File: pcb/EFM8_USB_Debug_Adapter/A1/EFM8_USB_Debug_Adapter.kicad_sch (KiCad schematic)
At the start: 27 parts, among them J100 EFM8 IDC Debug Header, J101 Conn_01x06, J110 2137160001, J120 31230102, J130 EFM8 USB 8-Bit Debug Header, J131 Conn_01x02_Male, Q110 SI3443CDV-T1-GE3, Q111 DMMT5401, Q120 SI3443CDV-T1-GE3, Q121 DMMT5401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

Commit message: Erstes Layout
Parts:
- removed J101: Conn_01x06, Connector_PinHeader_2.54mm:PinHeader_1x06_P2.54mm_Vertical, symbol Connector_Generic:Conn_01x06
- added J111: TTL-232R Header, Connector_PinHeader_2.54mm:PinHeader_1x06_P2.54mm_Vertical, symbol Connector_Special_Purpose_User:TTL-232R Header
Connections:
- net GND: now also J111.1 (GND)
- net UART_RX: now also J111.5 (RXD)
- net UART_TX: now also J111.4 (TXD)

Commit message: PCB bearbeitet, FreeCAD Projet angelegt
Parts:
- removed F110: 0805L110SLxx, Fuse:Fuse_0805_2012Metric_Pad1.15x1.40mm_HandSolder, symbol Fuse_User:0805L110SLxx
- removed J131: Conn_01x02_Male, Connector_PinHeader_2.54mm:PinHeader_1x02_P2.54mm_Vertical, symbol Connector:Conn_01x02_Male
- added D111, D121, D131: 150080SS75000, LED_SMD:LED_0805_2012Metric_Pad1.15x1.40mm_HandSolder, symbol LED_User:150080SS75000
- added F110: 0ZCJ0110FF2E, Fuse:Fuse_1206_3216Metric_Pad1.42x1.75mm_HandSolder, symbol Fuse_User:0ZCJ0110FF2E
- added JP130: SolderJumper_2_Bridged, Jumper:SolderJumper-2_P1.3mm_Bridged_RoundedPad1.0x1.5mm, symbol Jumper:SolderJumper_2_Bridged
- added R115, R123, R133: 2k,0603, Resistor_SMD:R_0603_1608Metric_Pad0.98x0.95mm_HandSolder, symbol Resistor_User:2k,0603
- D110, D120, D130: value LTST-C191TGKT -> 150080SS75000; footprint LED_SMD:LED_0603_1608Metric_Pad1.05x0.95mm_HandSolder -> LED_SMD:LED_0805_2012Metric_Pad1.15x1.40mm_HandSolder; symbol LED_User:LTST-C191TGKT -> LED_User:150080SS75000; Info Green -> Red; Manufacturer Lite-On -> Wurth Elektronik; SPN 160-1888-1-ND -> 732-4985-1-ND
- J100: value EFM8 IDC Debug Header -> EFM8_IDC_Debug_Header_Horizontal; footprint Connector_User:IDC-Header_2x03_P2.54mm_Vertical_61200621621 -> Connector_User:IDC-Header_2x03_P2.54mm_Horizontal_61200621721; symbol Connector_Special_Purpose_User:EFM8 IDC Debug Header -> Connector_Special_Purpose_User:EFM8_IDC_Debug_Header_Horizontal; MPN 61200621621 -> 61200621721; SPN 732-5394-ND -> 732-5404-ND
- J111: value TTL-232R Header -> TTL-232R_Header_Horizontal; footprint Connector_PinHeader_2.54mm:PinHeader_1x06_P2.54mm_Vertical -> Connector_PinHeader_2.54mm:PinHeader_1x06_P2.54mm_Horizontal; symbol Connector_Special_Purpose_User:TTL-232R Header -> Connector_Special_Purpose_User:TTL-232R_Header_Horizontal; MPN 61300611121 -> 61300611021; Pretty Value 1 01x06 Header -> 01x06 Header, Vertical; SPN 732-5319-ND -> 732-5339-ND
- J130: value EFM8 USB 8-Bit Debug Header -> EFM8_USB_8-Bit_Debug_Header_Horizontal; footprint Connector_User:IDC-Header_2x05_P2.54mm_Vertical_61201021621 -> Connector_User:IDC-Header_2x05_P2.54mm_Horizontal_61201021721; symbol Connector_Special_Purpose_User:EFM8 USB 8-Bit Debug Header -> Connector_Special_Purpose_User:EFM8_USB_8-Bit_Debug_Header_Horizontal; MPN 61201021621 -> 61201021721; SPN 732-2094-ND -> 732-2098-ND
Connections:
- net Ext_PSU_Power: now also D121.2 (A)
- net Ext_USB_Power: now also F110.1
- net GND: now also R115.2, R123.2, R133.2
- net Prog_USB_Power: now also JP130.1 (A)
- net Ext_USB_Power_Fused: now reaches D110.2 (A), Q110.1 (D), Q110.2 (D), Q110.5 (D), Q110.6 (D), Q111.6 (E1)
- net Ext_USB_Power_Fused: now also D111.2 (A), F110.2
- net at D130.2 (A), Q130.1 (D), Q130.2 (D)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: now also D131.2 (A), JP130.2 (B)
- new net: D131.1 (K), R133.1
- new net: D121.1 (K), R123.1
- new net: D111.1 (K), R115.1
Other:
- moved on the sheet: D110, D120, D130, J100, J110, J111, J120, J130, Q110, Q111, Q120, Q121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

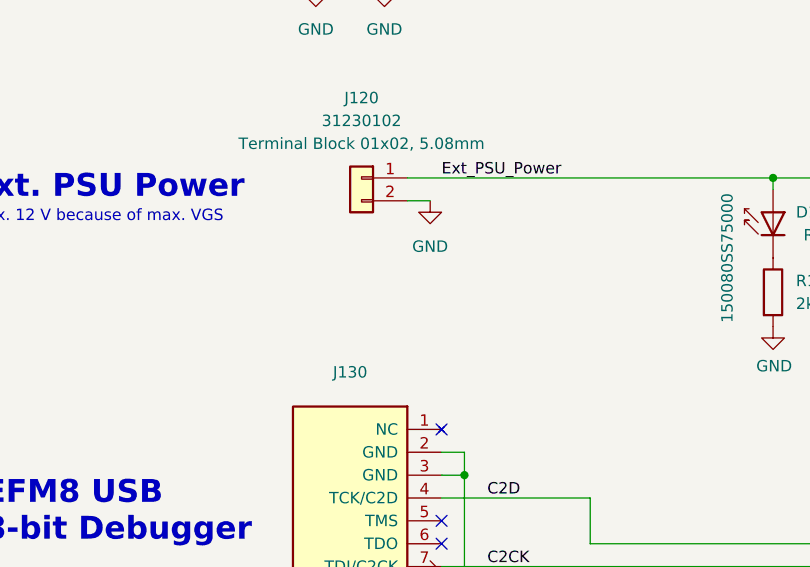
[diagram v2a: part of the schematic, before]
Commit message: Gehäuse bearbeitet
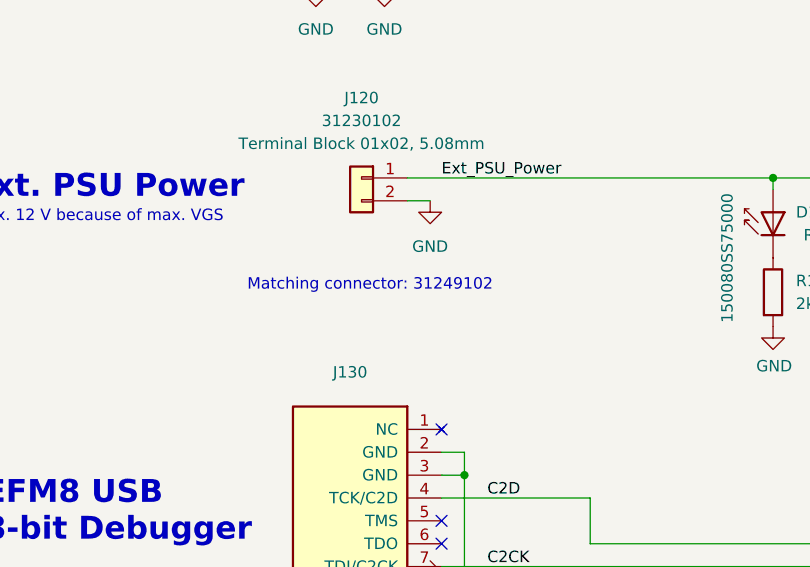
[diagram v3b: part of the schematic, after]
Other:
- note added: "Matching connector: 31249102"
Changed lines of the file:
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@@
+    (effects (font (size 1.27 1.27)) (justify left bottom))
+  )
+  (text "Matching connector: 31249102" (at 44.45 95.25 0)
     (effects (font (size 1.27 1.27)) (justify left bottom))
   )
@@
       (effects (font (size 1.27 1.27)) hide)
     )
-    (property "Datasheet" "https://www.metz-connect.com/html/overlay:service:download.en.html?filepath=db%3Aproducts%2Fdocid%3A8a8a80ea821fbff0018315b584d92138.de.1&fileurl=312301%2F873130.PDF" (id 3) (at 57.15 100.33 0)
-      (effects (font (size 1.27 1.27)) hide)
-    )
+    (property "Datasheet" "https://www.metz-connect.com/externalfiles/312301/873130.PDF" (id 3) (at 57.15 100.33 0)
+      (effects (font (size 1.27 1.27)) hide)
+    )

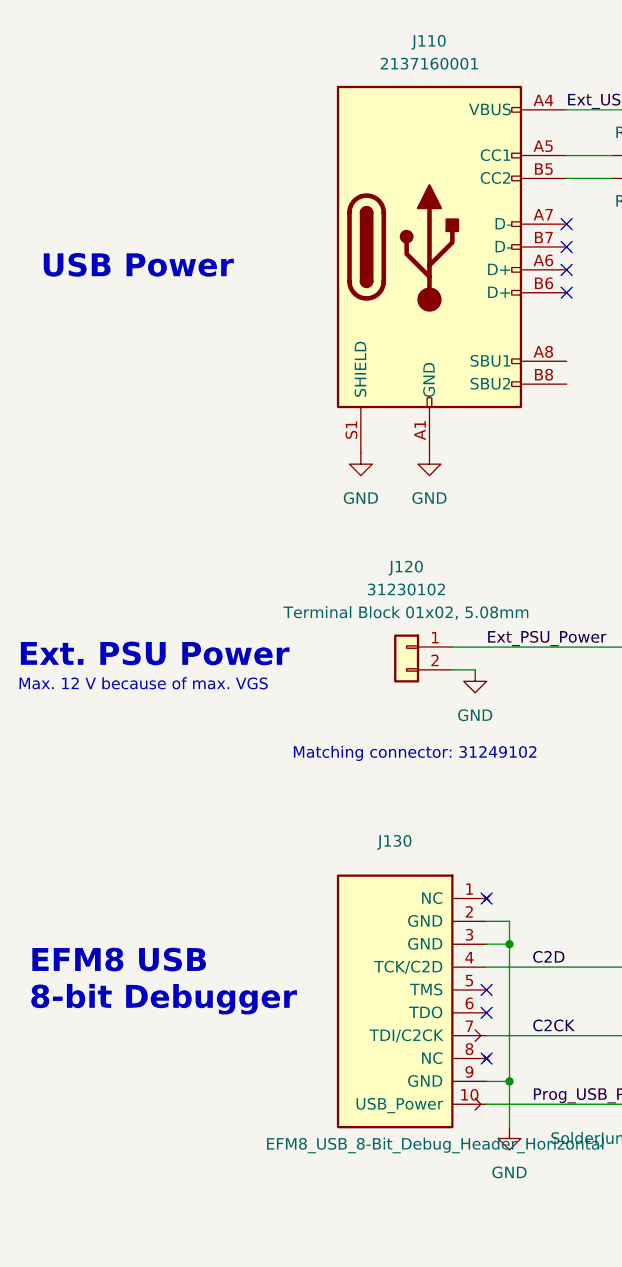
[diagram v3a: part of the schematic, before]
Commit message: Light Pipes in KiCad hinzugefügt
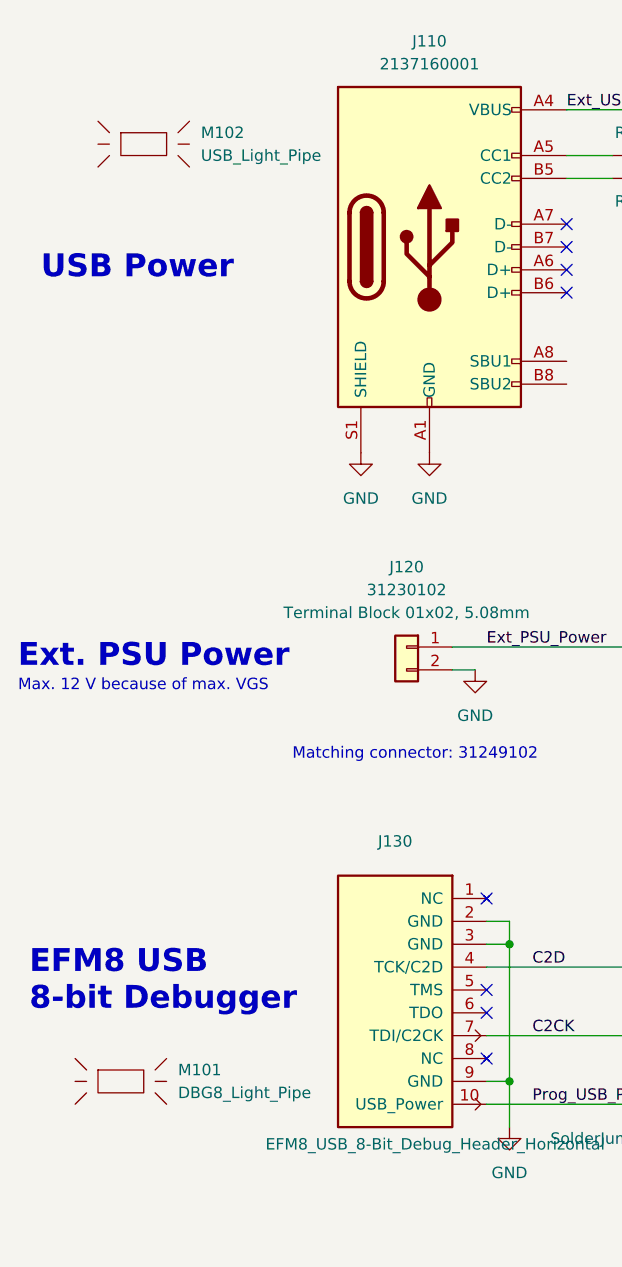
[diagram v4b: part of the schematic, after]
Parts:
- added M101: DBG8_Light_Pipe, Mechanical_User:DBG8_CON_Light_Pipe, symbol Mechanical_User:DBG8_Light_Pipe
- added M102: USB_Light_Pipe, Mechanical_User:USB_CON_Light_Pipe, symbol Mechanical_User:USB_Light_Pipe
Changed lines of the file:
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@@
     (pin "1")
+  )
+  (symbol (lib_id "Mechanical_User:USB_Light_Pipe") (at 27.94 26.67 0) (unit 1)
+    (in_bom yes) (on_board yes) (fields_autoplaced)
+    (property "Reference" "M102" (id 0) (at 34.29 25.3999 0)
+      (effects (font (size 1.27 1.27)) (justify left))
+    )
+    (property "Value" "USB_Light_Pipe" (id 1) (at 34.29 27.9399 0)
+      (effects (font (size 1.27 1.27)) (justify left))
+    )
+    (property "Footprint" "Mechanical_User:USB_CON_Light_Pipe" (id 2) (at 27.94 33.02 0)
+      (effects (font (size 1.27 1.27)) hide)
+    )
+    (property "Datasheet" "" (id 3) (at 27.94 26.67 0)
+      (effects (font (size 1.27 1.27)) hide)
+    )
   )
   (symbol (lib_id "Resistor_User:5.1k,0603") (at 83.82 27.94 90) (unit 1)
@@
     (pin "1")
     (pin "2")
+  )
+  (symbol (lib_id "Mechanical_User:DBG8_Light_Pipe") (at 25.4 130.81 0) (unit 1)
+    (in_bom yes) (on_board yes) (fields_autoplaced)
+    (property "Reference" "M101" (id 0) (at 31.75 129.5399 0)
+      (effects (font (size 1.27 1.27)) (justify left))
+    )
+    (property "Value" "DBG8_Light_Pipe" (id 1) (at 31.75 132.0799 0)
+      (effects (font (size 1.27 1.27)) (justify left))
+    )
+    (property "Footprint" "Mechanical_User:DBG8_CON_Light_Pipe" (id 2) (at 25.4 137.16 0)
+      (effects (font (size 1.27 1.27)) hide)
+    )
+    (property "Datasheet" "" (id 3) (at 25.4 130.81 0)
+      (effects (font (size 1.27 1.27)) hide)
+    )
   )
   (symbol (lib_id "power:GND") (at 149.86 166.37 0) (unit 1)
@@
       (reference "JP130") (unit 1) (value "SolderJumper_2_Bridged") (footprint "Jumper:SolderJumper-2_P1.3mm_Bridged_RoundedPad1.0x1.5mm")
     )
+    (path "/a1ba61a6-05d5-4139-8461-75a55b58685e"
+      (reference "M101") (unit 1) (value "DBG8_Light_Pipe") (footprint "Mechanical_User:DBG8_CON_Light_Pipe")
+    )
+    (path "/202d9ec9-e487-4b5e-9a3f-823061d2216d"
+      (reference "M102") (unit 1) (value "USB_Light_Pipe") (footprint "Mechanical_User:USB_CON_Light_Pipe")
+    )
     (path "/407789ef-b748-4a75-acb1-ac2bbc66b346"

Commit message: Lightpipes aktualisiert
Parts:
- added M120: PSU_Light_Pipe, Mechanical_User:PSU_CON_Light_Pipe, symbol Mechanical_User:PSU_Light_Pipe
- renumbered M102 to M110, M101 to M130
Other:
- moved on the sheet: M110
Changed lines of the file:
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@@
     (pin "1")
   )
-  (symbol (lib_id "Mechanical_User:USB_Light_Pipe") (at 27.94 26.67 0) (unit 1)
-    (in_bom yes) (on_board yes) (fields_autoplaced)
-    (property "Reference" "M102" (id 0) (at 34.29 25.3999 0)
-      (effects (font (size 1.27 1.27)) (justify left))
-    )
-    (property "Value" "USB_Light_Pipe" (id 1) (at 34.29 27.9399 0)
-      (effects (font (size 1.27 1.27)) (justify left))
-    )
-    (property "Footprint" "Mechanical_User:USB_CON_Light_Pipe" (id 2) (at 27.94 33.02 0)
-      (effects (font (size 1.27 1.27)) hide)
-    )
-    (property "Datasheet" "" (id 3) (at 27.94 26.67 0)
+  (symbol (lib_id "Mechanical_User:USB_Light_Pipe") (at 25.4 26.67 0) (unit 1)
+    (in_bom yes) (on_board yes) (fields_autoplaced)
+    (property "Reference" "M110" (id 0) (at 31.75 25.3999 0)
+      (effects (font (size 1.27 1.27)) (justify left))
+    )
+    (property "Value" "USB_Light_Pipe" (id 1) (at 31.75 27.9399 0)
+      (effects (font (size 1.27 1.27)) (justify left))
+    )
+    (property "Footprint" "Mechanical_User:USB_CON_Light_Pipe" (id 2) (at 25.4 33.02 0)
+      (effects (font (size 1.27 1.27)) hide)
+    )
+    (property "Datasheet" "" (id 3) (at 25.4 26.67 0)
       (effects (font (size 1.27 1.27)) hide)
     )
@@
   (symbol (lib_id "Mechanical_User:DBG8_Light_Pipe") (at 25.4 130.81 0) (unit 1)
     (in_bom yes) (on_board yes) (fields_autoplaced)
-    (property "Reference" "M101" (id 0) (at 31.75 129.5399 0)
+    (property "Reference" "M130" (id 0) (at 31.75 129.5399 0)
       (effects (font (size 1.27 1.27)) (justify left))
     )
@@
     (pin "8")
     (pin "9")
+  )
+  (symbol (lib_id "Mechanical_User:PSU_Light_Pipe") (at 25.4 73.66 0) (unit 1)
+    (in_bom yes) (on_board yes) (fields_autoplaced)
+    (property "Reference" "M120" (id 0) (at 31.75 72.3899 0)
+      (effects (font (size 1.27 1.27)) (justify left))
+    )
+    (property "Value" "PSU_Light_Pipe" (id 1) (at 31.75 74.9299 0)
+      (effects (font (size 1.27 1.27)) (justify left))
+    )
+    (property "Footprint" "Mechanical_User:PSU_CON_Light_Pipe" (id 2) (at 25.4 80.01 0)
+      (effects (font (size 1.27 1.27)) hide)
+    )
+    (property "Datasheet" "" (id 3) (at 25.4 73.66 0)
+      (effects (font (size 1.27 1.27)) hide)
+    )
   )
   (symbol (lib_id "Connector_User:2137160001") (at 59.69 38.1 0) (unit 1)
@@
       (reference "JP130") (unit 1) (value "SolderJumper_2_Bridged") (footprint "Jumper:SolderJumper-2_P1.3mm_Bridged_RoundedPad1.0x1.5mm")
     )
+    (path "/202d9ec9-e487-4b5e-9a3f-823061d2216d"
+      (reference "M110") (unit 1) (value "USB_Light_Pipe") (footprint "Mechanical_User:USB_CON_Light_Pipe")
+    )
+    (path "/dd8ebda5-d5b5-480a-aef5-1ead370bce60"
+      (reference "M120") (unit 1) (value "PSU_Light_Pipe") (footprint "Mechanical_User:PSU_CON_Light_Pipe")
+    )
     (path "/a1ba61a6-05d5-4139-8461-75a55b58685e"
-      (reference "M101") (unit 1) (value "DBG8_Light_Pipe") (footprint "Mechanical_User:DBG8_CON_Light_Pipe")
-    )
-    (path "/202d9ec9-e487-4b5e-9a3f-823061d2216d"
-      (reference "M102") (unit 1) (value "USB_Light_Pipe") (footprint "Mechanical_User:USB_CON_Light_Pipe")
+      (reference "M130") (unit 1) (value "DBG8_Light_Pipe") (footprint "Mechanical_User:DBG8_CON_Light_Pipe")
     )
     (path "/407789ef-b748-4a75-acb1-ac2bbc66b346"

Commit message: PCB bearbeitet
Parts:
- removed JP130: SolderJumper_2_Bridged, Jumper:SolderJumper-2_P1.3mm_Bridged_RoundedPad1.0x1.5mm, symbol Jumper:SolderJumper_2_Bridged
- added J131: Header_01x02_Wurth_61300211121, Connector_PinHeader_2.54mm:PinHeader_1x02_P2.54mm_Vertical, symbol Connector_User:Header_01x02_Wurth_61300211121
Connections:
- net Prog_USB_Power: now also J131.2 (Pin_2)
- net at D130.2 (A), D131.2 (A), Q130.1 (D)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: now also J131.1 (Pin_1)
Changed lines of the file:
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@@
     (stroke (width 0) (type default) (color 0 0 0 0))
   )
-  (wire (pts (xy 93.98 133.35) (xy 102.87 133.35))
+  (wire (pts (xy 91.44 133.35) (xy 102.87 133.35))
     (stroke (width 0) (type default) (color 0 0 0 0))
   )
@@
     (stroke (width 0) (type default) (color 0 0 0 0))
   )
+  (wire (pts (xy 66.04 133.35) (xy 88.9 133.35))
+    (stroke (width 0) (type default) (color 0 0 0 0))
+  )
   (wire (pts (xy 179.07 133.35) (xy 179.07 82.55))
     (stroke (width 0) (type default) (color 0 0 0 0))
@@
   )
   (wire (pts (xy 161.29 43.18) (xy 161.29 46.99))
-    (stroke (width 0) (type default) (color 0 0 0 0))
-  )
-  (wire (pts (xy 66.04 133.35) (xy 86.36 133.35))
     (stroke (width 0) (type default) (color 0 0 0 0))
   )
@@
     (pin "4")
   )
-  (symbol (lib_id "Jumper:SolderJumper_2_Bridged") (at 90.17 133.35 0) (unit 1)
-    (in_bom yes) (on_board yes)
-    (property "Reference" "JP130" (id 0) (at 90.17 130.81 0))
-    (property "Value" "SolderJumper_2_Bridged" (id 1) (at 83.82 137.16 0))
-    (property "Footprint" "Jumper:SolderJumper-2_P1.3mm_Bridged_RoundedPad1.0x1.5mm" (id 2) (at 90.17 133.35 0)
-      (effects (font (size 1.27 1.27)) hide)
-    )
-    (property "Datasheet" "~" (id 3) (at 90.17 133.35 0)
-      (effects (font (size 1.27 1.27)) hide)
-    )
-    (pin "1")
-    (pin "2")
-  )
   (symbol (lib_id "power:GND") (at 161.29 166.37 0) (unit 1)
     (in_bom yes) (on_board yes)
@@
     (pin "1")
   )
+  (symbol (lib_id "Connector_User:Header_01x02_Wurth_61300211121") (at 90.17 138.43 270) (unit 1)
+    (in_bom yes) (on_board yes)
+    (property "Reference" "J131" (id 0) (at 93.98 135.8899 90)
+      (effects (font (size 1.27 1.27)) (justify left))
+    )
+    (property "Value" "Header_01x02_Wurth_61300211121" (id 1) (at 69.85 146.05 90)
+      (effects (font (size 1.27 1.27)) (justify left) hide)
+    )
+    (property "Footprint" "Connector_PinHeader_2.54mm:PinHeader_1x02_P2.54mm_Vertical" (id 2) (at 79.375 137.795 0)
+      (effects (font (size 1.27 1.27)) hide)
+    )
+    (property "Datasheet" "https://www.we-online.com/katalog/datasheet/61300211121.pdf" (id 3) (at 79.375 137.795 0)
+      (effects (font (size 1.27 1.27)) hide)
+    )
+    (property "Manufacturer" "Wurth Electronics" (id 4) (at 80.01 138.43 0)
+      (effects (font (size 1.27 1.27)) hide)
+    )
+    (property "MPN" "61300211121" (id 5) (at 80.01 138.43 0)
+      (effects (font (size 1.27 1.27)) hide)
+    )
+    (property "Supplier" "Digi-Key" (id 6) (at 79.375 138.43 0)
+      (effects (font (size 1.27 1.27)) hide)
+    )
+    (property "SPN" "732-5315-ND" (id 7) (at 80.01 138.43 0)
+      (effects (font (size 1.27 1.27)) hide)
+    )
+    (property "Pretty Value" "01x02 Header" (id 8) (at 83.82 140.97 90)
+      (effects (font (size 1.27 1.27)) (justify left))
+    )
+    (pin "1")
+    (pin "2")
+  )
   (symbol (lib_id "power:GND") (at 92.71 31.75 0) (unit 1)
     (in_bom yes) (on_board yes) (fields_autoplaced)
@@
     (in_bom yes) (on_board yes)
     (property "Reference" "J130" (id 0) (at 55.88 104.14 0))
-    (property "Value" "EFM8_USB_8-Bit_Debug_Header_Horizontal" (id 1) (at 60.325 137.795 0))
+    (property "Value" "EFM8_USB_8-Bit_Debug_Header_Horizontal" (id 1) (at 57.15 106.68 0))
     (property "Footprint" "Connector_User:IDC-Header_2x05_P2.54mm_Horizontal_61201021721" (id 2) (at 59.69 142.24 0)
       (effects (font (size 1.27 1.27)) hide)
@@
       (reference "J130") (unit 1) (value "EFM8_USB_8-Bit_Debug_Header_Horizontal") (footprint "Connector_User:IDC-Header_2x05_P2.54mm_Horizontal_61201021721")
     )
-    (path "/4371cedd-a894-45a7-8f2e-b664b567a667"
-      (reference "JP130") (unit 1) (value "SolderJumper_2_Bridged") (footprint "Jumper:SolderJumper-2_P1.3mm_Bridged_RoundedPad1.0x1.5mm")
+    (path "/881022a7-e436-4116-b053-fa114a13f2a1"
+      (reference "J131") (unit 1) (value "Header_01x02_Wurth_61300211121") (footprint "Connector_PinHeader_2.54mm:PinHeader_1x02_P2.54mm_Vertical")
     )
     (path "/202d9ec9-e487-4b5e-9a3f-823061d2216d"

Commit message: PCB Rev. A1
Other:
- company: (none) -> flomo
- title: (none) -> EFM8 USB Debug Adapter
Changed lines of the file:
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@@
 (kicad_sch (version 20211123) (generator eeschema)
   (paper "A4")
+  (title_block
+    (title "EFM8 USB Debug Adapter")
+    (date "2022-11-08")
+    (rev "A1")
+    (company "flomo")
+  )
   (junction (at 161.29 106.68) (diameter 0) (color 0 0 0 0)
   )
@@
   (no_connect (at 74.93 40.64))
   (no_connect (at 74.93 43.18))
+  (no_connect (at 74.93 53.34))
+  (no_connect (at 74.93 50.8))
   (no_connect (at 66.04 176.53))
   (no_connect (at 66.04 173.99))
   (no_connect (at 66.04 184.15))
-  (no_connect (at 66.04 128.27))
   (no_connect (at 66.04 123.19))
   (no_connect (at 66.04 120.65))
-  (no_connect (at 66.04 110.49))
   (wire (pts (xy 198.12 120.65) (xy 213.36 120.65))
     (stroke (width 0) (type default) (color 0 0 0 0))
